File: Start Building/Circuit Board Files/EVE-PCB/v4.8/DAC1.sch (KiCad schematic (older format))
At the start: 26 parts, among them Q2 ULN2803ADWR, Q3 ULN2803ADWR, Q8 DMN6140LQ-7, Q9 DMN6140LQ-7, U7 MCP23017-E/SO

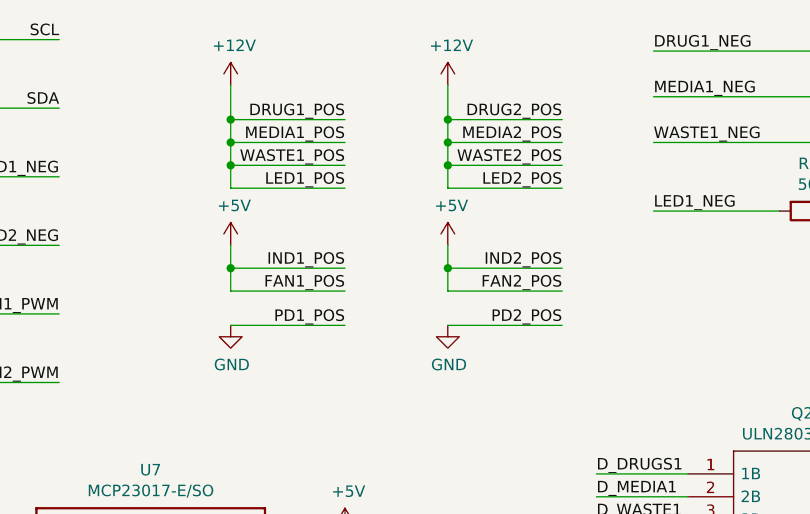
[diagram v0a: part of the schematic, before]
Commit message: Bump PCB version to 4.81
- Fixed voltages for fan and LED
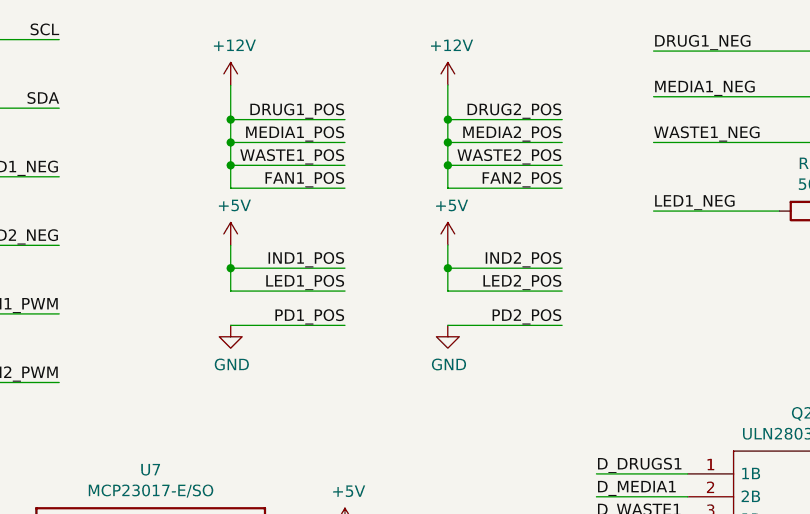
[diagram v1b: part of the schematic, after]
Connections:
- net +12V: now also L1.10, L2.10; no longer L1.11, L2.11
- net +5V: now also L1.11, L2.11; no longer L1.10, L2.10
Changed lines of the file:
@@
 $Descr A4 11693 8268
 encoding utf-8
-Sheet 2 3
+Sheet 3 3
 Title ""
 Date ""
@@
 WASTE1_POS
 Text Label 3100 1400 2    50   ~ 0
-LED1_POS
+FAN1_POS
 $Comp
 L EVE-PCB-V4-rescue:+12V-power-EVE-PCB-rescue #PWR034
@@
 WASTE2_POS
 Text Label 4050 1400 2    50   ~ 0
-LED2_POS
+FAN2_POS
 $Comp
 L EVE-PCB-V4-rescue:+12V-power-EVE-PCB-rescue #PWR039
@@
 	3100 1850 2600 1850
 Text Label 3100 1850 2    50   ~ 0
-FAN1_POS
+LED1_POS
 Wire Wire Line
 	4050 1850 3550 1850
 Text Label 4050 1850 2    50   ~ 0
-FAN2_POS
+LED2_POS
 Wire Wire Line
 	3550 1750 3550 1850

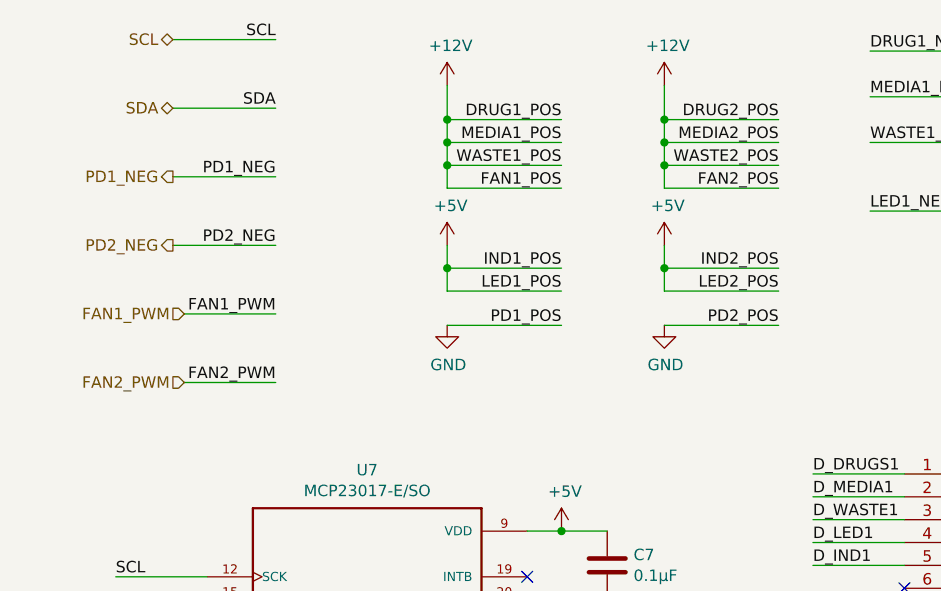
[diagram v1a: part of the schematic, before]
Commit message: Bump PCB to version 4.82
- Update schematic to use V_ref as PD positive terminal.
- Update PCB to allow for this change.
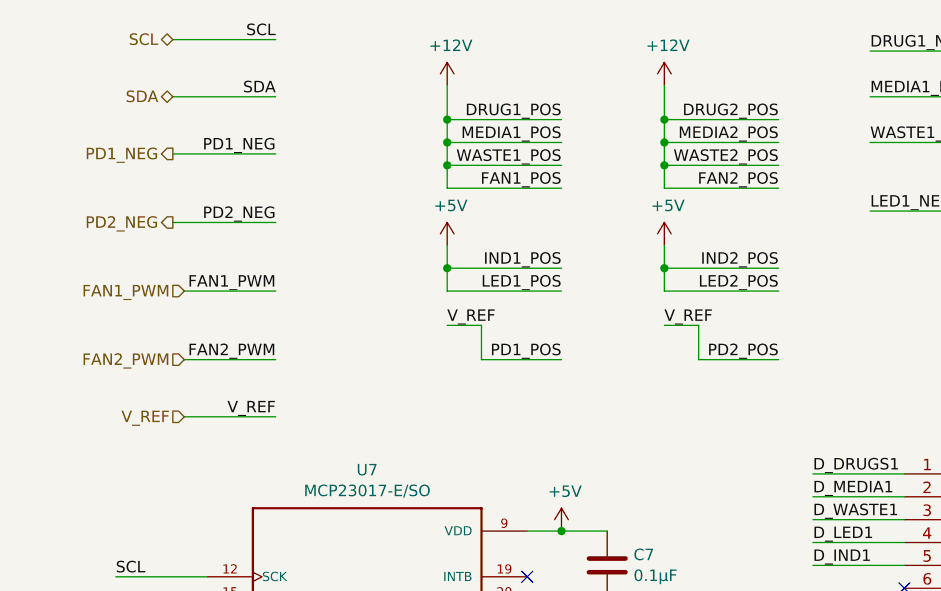
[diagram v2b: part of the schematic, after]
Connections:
- net GND: no longer L1.12, L2.12
- new net V_REF: L1.12, L2.12
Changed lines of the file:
@@
 Text HLabel 1400 750  0    50   BiDi ~ 0
 SCL
-Text HLabel 1400 1050 0    50   BiDi ~ 0
+Text HLabel 1400 1000 0    50   BiDi ~ 0
 SDA
 Text Label 1850 750  2    50   ~ 0
 SCL
-Text Label 1850 1050 2    50   ~ 0
+Text Label 1850 1000 2    50   ~ 0
 SDA
 Wire Wire Line
@@
 	1400 750  1850 750
 Wire Wire Line
-	1400 1050 1850 1050
+	1400 1000 1850 1000
 NoConn ~ 2950 4400
 NoConn ~ 1550 4500
@@
 Wire Wire Line
 	7150 5000 7650 5000
-Text Label 3100 2000 2    50   ~ 0
-PD1_POS
-$Comp
-L EVE-PCB-V4-rescue:GND-power-EVE-PCB-rescue #PWR035
-U 1 1 5CCCBCCC
-P 2600 2000
-F 0 "#PWR035" H 2600 1750 50  0001 C CNN
-F 1 "GND" H 2605 1827 50  0000 C CNN
-F 2 "" H 2600 2000 50  0001 C CNN
-F 3 "" H 2600 2000 50  0001 C CNN
-	1    2600 2000
-	1    0    0    -1
-$EndComp
-Wire Wire Line
-	2600 2000 3100 2000
-Text Label 4050 2000 2    50   ~ 0
-PD2_POS
-$Comp
-L EVE-PCB-V4-rescue:GND-power-EVE-PCB-rescue #PWR040
-U 1 1 5CCEE678
-P 3550 2000
-F 0 "#PWR040" H 3550 1750 50  0001 C CNN
-F 1 "GND" H 3555 1827 50  0000 C CNN
-F 2 "" H 3550 2000 50  0001 C CNN
-F 3 "" H 3550 2000 50  0001 C CNN
-	1    3550 2000
-	1    0    0    -1
-$EndComp
-Wire Wire Line
-	3550 2000 4050 2000
-Text Label 1850 1650 2    50   ~ 0
+Text Label 1850 1550 2    50   ~ 0
 PD2_NEG
-Text Label 1850 1350 2    50   ~ 0
+Text Label 1850 1250 2    50   ~ 0
 PD1_NEG
-Text HLabel 1400 1350 0    50   Output ~ 0
+Text HLabel 1400 1250 0    50   Output ~ 0
 PD1_NEG
-Text HLabel 1400 1650 0    50   Output ~ 0
+Text HLabel 1400 1550 0    50   Output ~ 0
 PD2_NEG
 Wire Wire Line
-	1400 1350 1850 1350
-Wire Wire Line
-	1400 1650 1850 1650
+	1400 1250 1850 1250
+Wire Wire Line
+	1400 1550 1850 1550
 $Comp
 L EVE-PCB-V4-rescue:C-Device-EVE-PCB-rescue C?
@@
 NoConn ~ 4600 4800
 NoConn ~ 4600 4900
-Text Label 1850 1950 2    50   ~ 0
+Text Label 1850 1850 2    50   ~ 0
 FAN1_PWM
-Text Label 1850 2250 2    50   ~ 0
+Text Label 1850 2150 2    50   ~ 0
 FAN2_PWM
 Wire Wire Line
-	1850 1950 1450 1950
-Wire Wire Line
-	1850 2250 1450 2250
-Text HLabel 1450 1950 0    50   Input ~ 0
+	1850 1850 1450 1850
+Wire Wire Line
+	1850 2150 1450 2150
+Text HLabel 1450 1850 0    50   Input ~ 0
 FAN1_PWM
-Text HLabel 1450 2250 0    50   Input ~ 0
+Text HLabel 1450 2150 0    50   Input ~ 0
 FAN2_PWM
 Text Label 9000 2000 2    50   ~ 0
@@
 	1    0    0    -1
 $EndComp
+Text HLabel 1450 2400 0    50   Input ~ 0
+V_REF
+Text Label 3100 2150 2    50   ~ 0
+PD1_POS
+Text Label 4050 2150 2    50   ~ 0
+PD2_POS
+Text Label 1850 2400 2    50   ~ 0
+V_REF
+Wire Wire Line
+	1850 2400 1450 2400
+Text Label 2600 2000 0    50   ~ 0
+V_REF
+Text Label 3550 2000 0    50   ~ 0
+V_REF
+Wire Wire Line
+	3550 2000 3700 2000
+Wire Wire Line
+	3700 2000 3700 2150
+Wire Wire Line
+	3700 2150 4050 2150
+Wire Wire Line
+	2600 2000 2750 2000
+Wire Wire Line
+	2750 2000 2750 2150
+Wire Wire Line
+	2750 2150 3100 2150
 $EndSCHEMATC
